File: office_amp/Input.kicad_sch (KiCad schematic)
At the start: 25 parts, among them J2 Conn_01x03_Female, J3 Conn_02x07_Odd_Even, J8 Conn_01x03_Female, K1 EC2-24NU, K2 EC2-24NU, K3 EC2-24NU, K4 EC2-24NU, Q4 BC850, Q5 BC850, U5 MH-M18

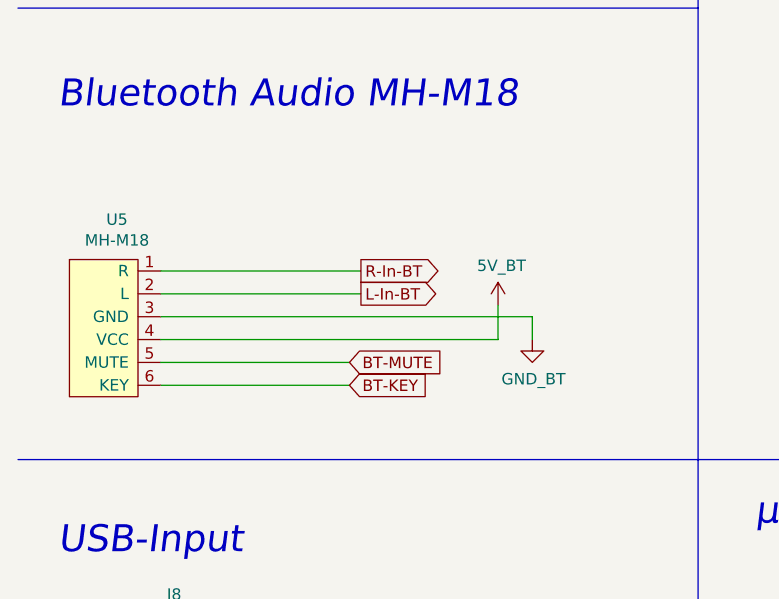
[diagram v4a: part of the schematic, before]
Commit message: Added bluetooth vcc filter, moved i2c pullups to controll board, added touch controller
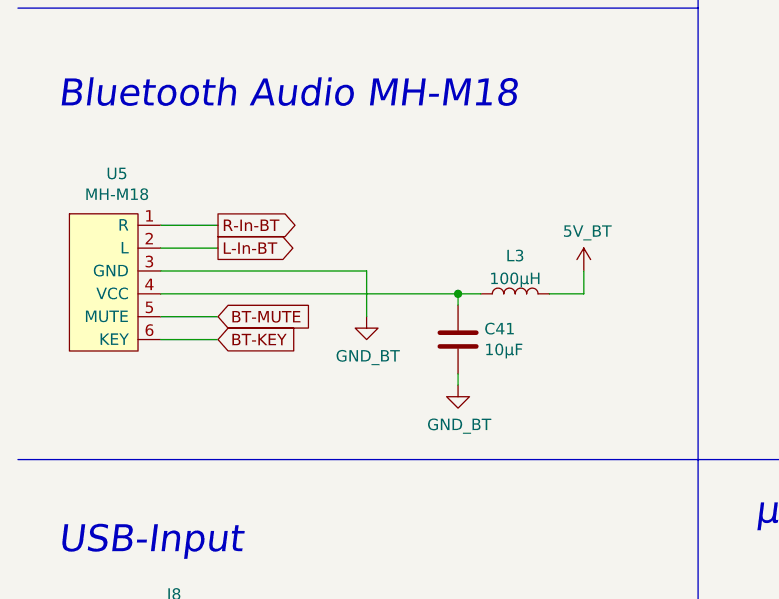
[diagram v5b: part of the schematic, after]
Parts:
- added C41: 10µF, Capacitor_SMD:C_0805_2012Metric_Pad1.18x1.45mm_HandSolder, symbol Device:C
- added L3: 100µH, Inductor_THT:L_Axial_L7.0mm_D3.3mm_P12.70mm_Horizontal_Fastron_MICC, symbol Device:L
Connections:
- net 5V_BT: now also L3.2; no longer U5.4 (VCC)
- net GND_BT: now also C41.2
- new net: C41.1, L3.1, U5.4 (VCC)
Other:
- moved on the sheet: U5

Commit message: Changes from testing
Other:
- note added: "relais in reihe"
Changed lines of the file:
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@@
     (effects (font (size 2.9972 2.9972) italic) (justify left bottom))
+  )
+  (text "relais in reihe" (at 151.765 82.55 0)
+    (effects (font (size 8 8)) (justify left bottom))
   )
   (global_label "L-In-An" (shape output) (at 64.77 35.56 0) (fields_autoplaced)

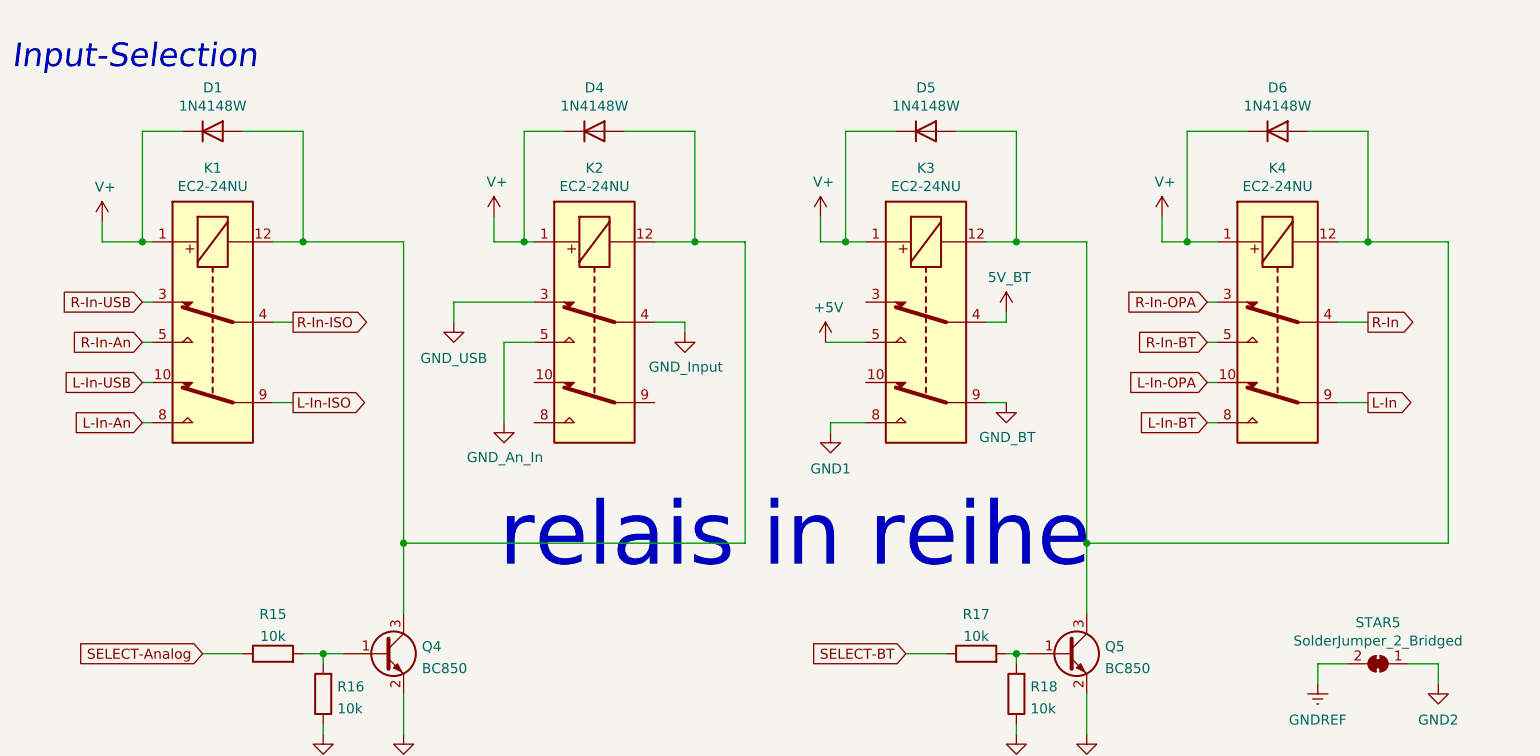
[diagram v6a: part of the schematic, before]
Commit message: Added CHanges from Testing, first layout V1.5
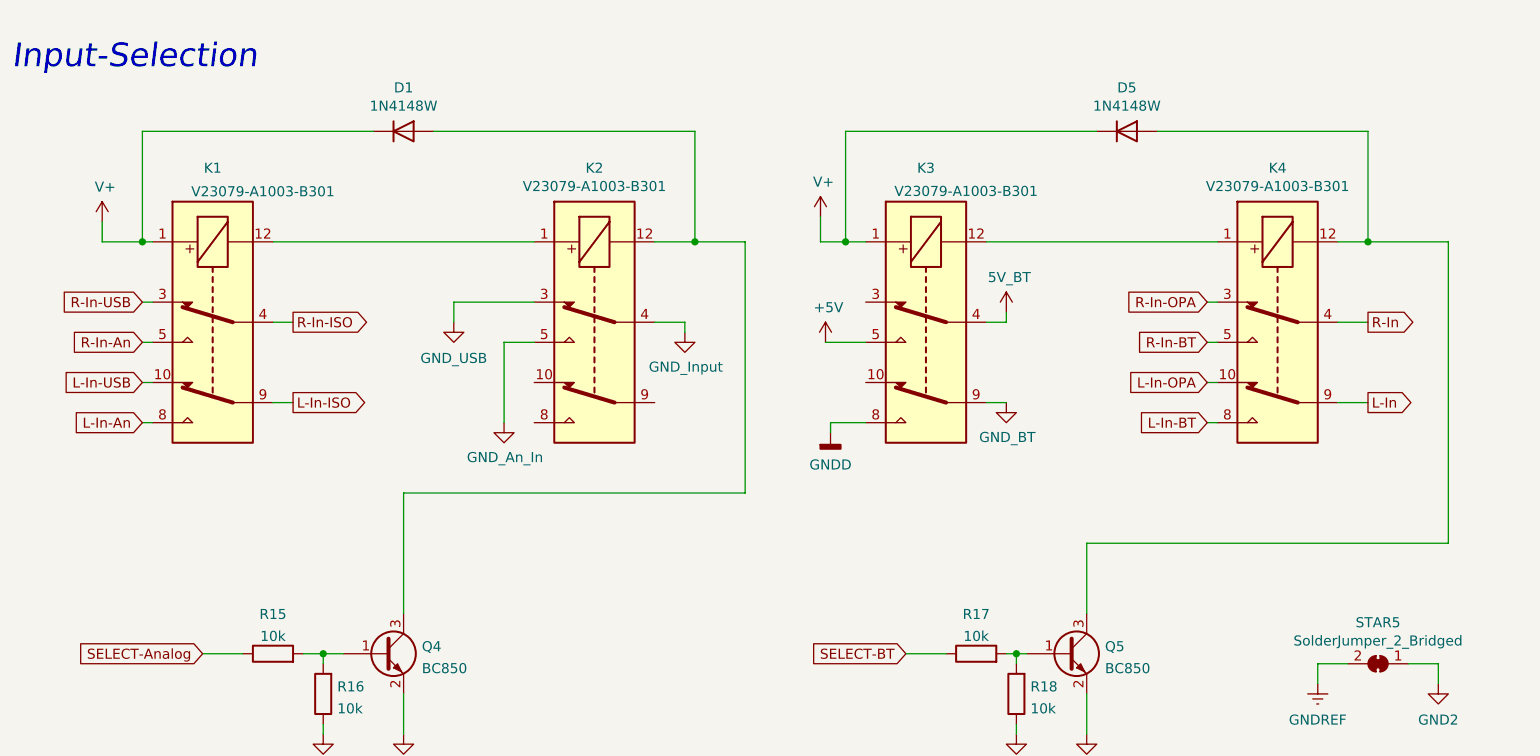
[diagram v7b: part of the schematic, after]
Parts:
- removed D4, D6: 1N4148W, Diode_SMD:D_SOD-123, symbol Diode:1N4148W
- K1, K2, K3, K4: value EC2-24NU -> V23079-A1003-B301
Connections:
- net GND1 is gone; now on net GNDD: K3.8
- net V+: no longer K2.1, K4.1
- net at D1.2 (A), K2.12, Q4.3 (C): no longer K1.12
- net at D5.2 (A), K4.12, Q5.3 (C): no longer K3.12
- new net: K1.12, K2.1
- new net: K3.12, K4.1
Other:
- note removed: "relais in reihe"
- moved on the sheet: D1, D5

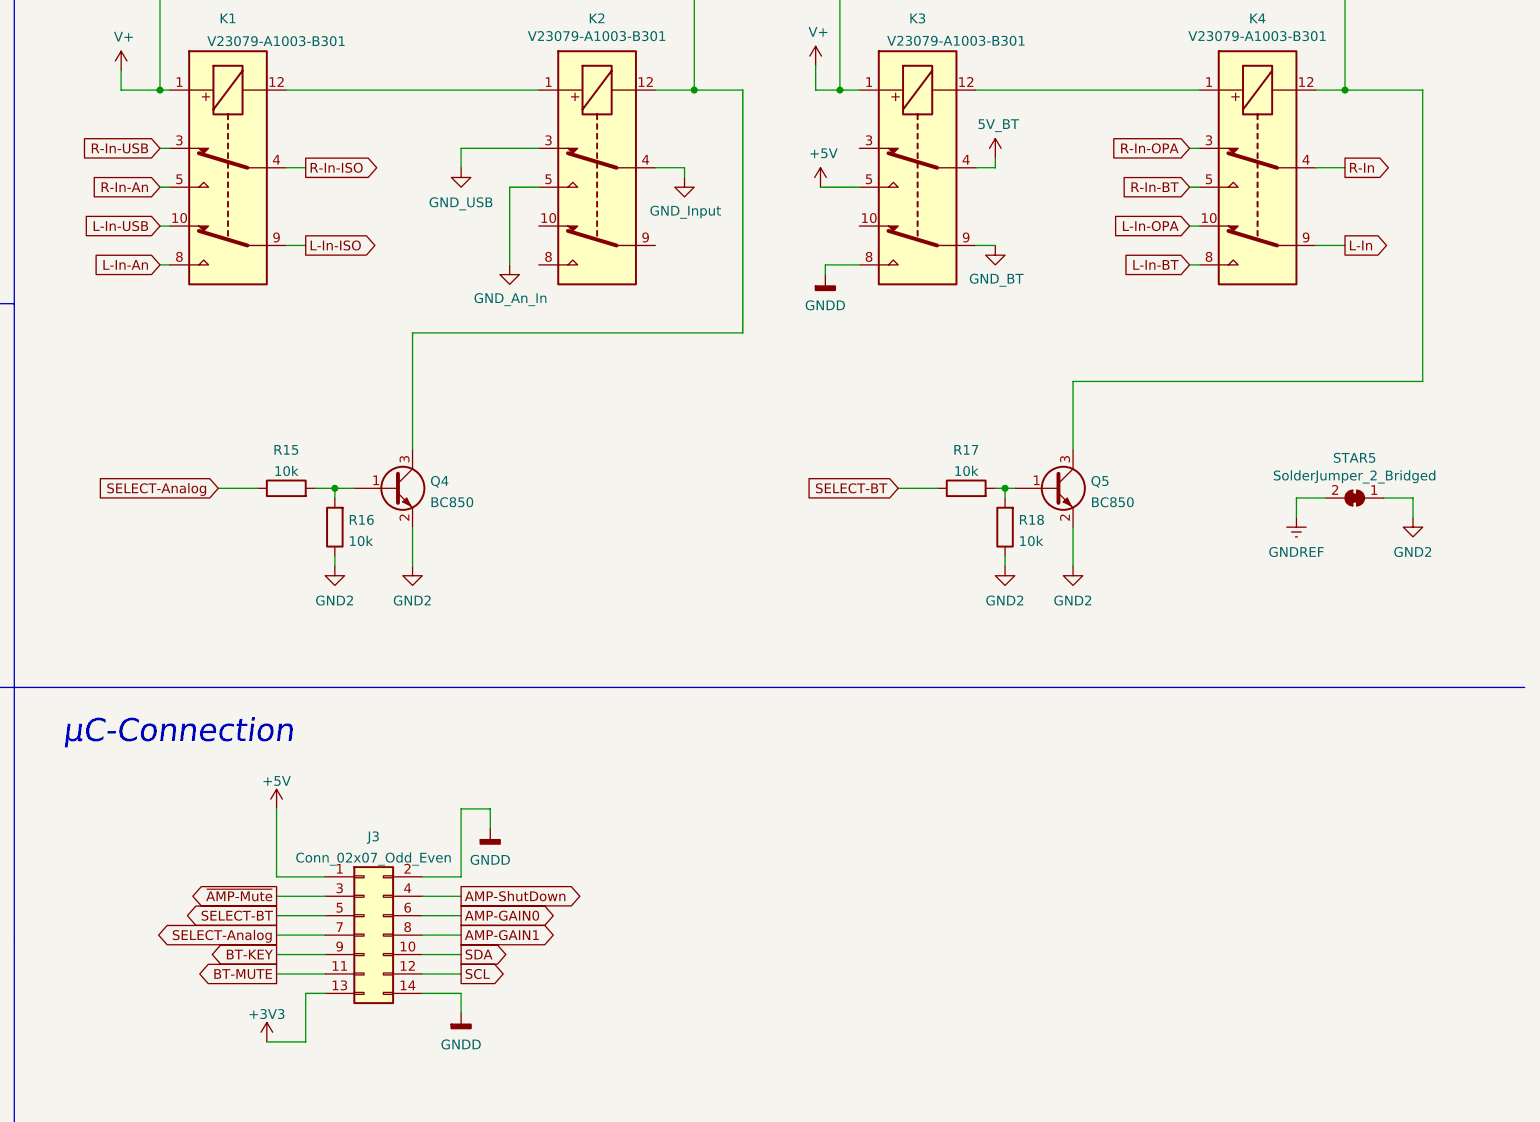
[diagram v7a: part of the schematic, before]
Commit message: Organized Schematic
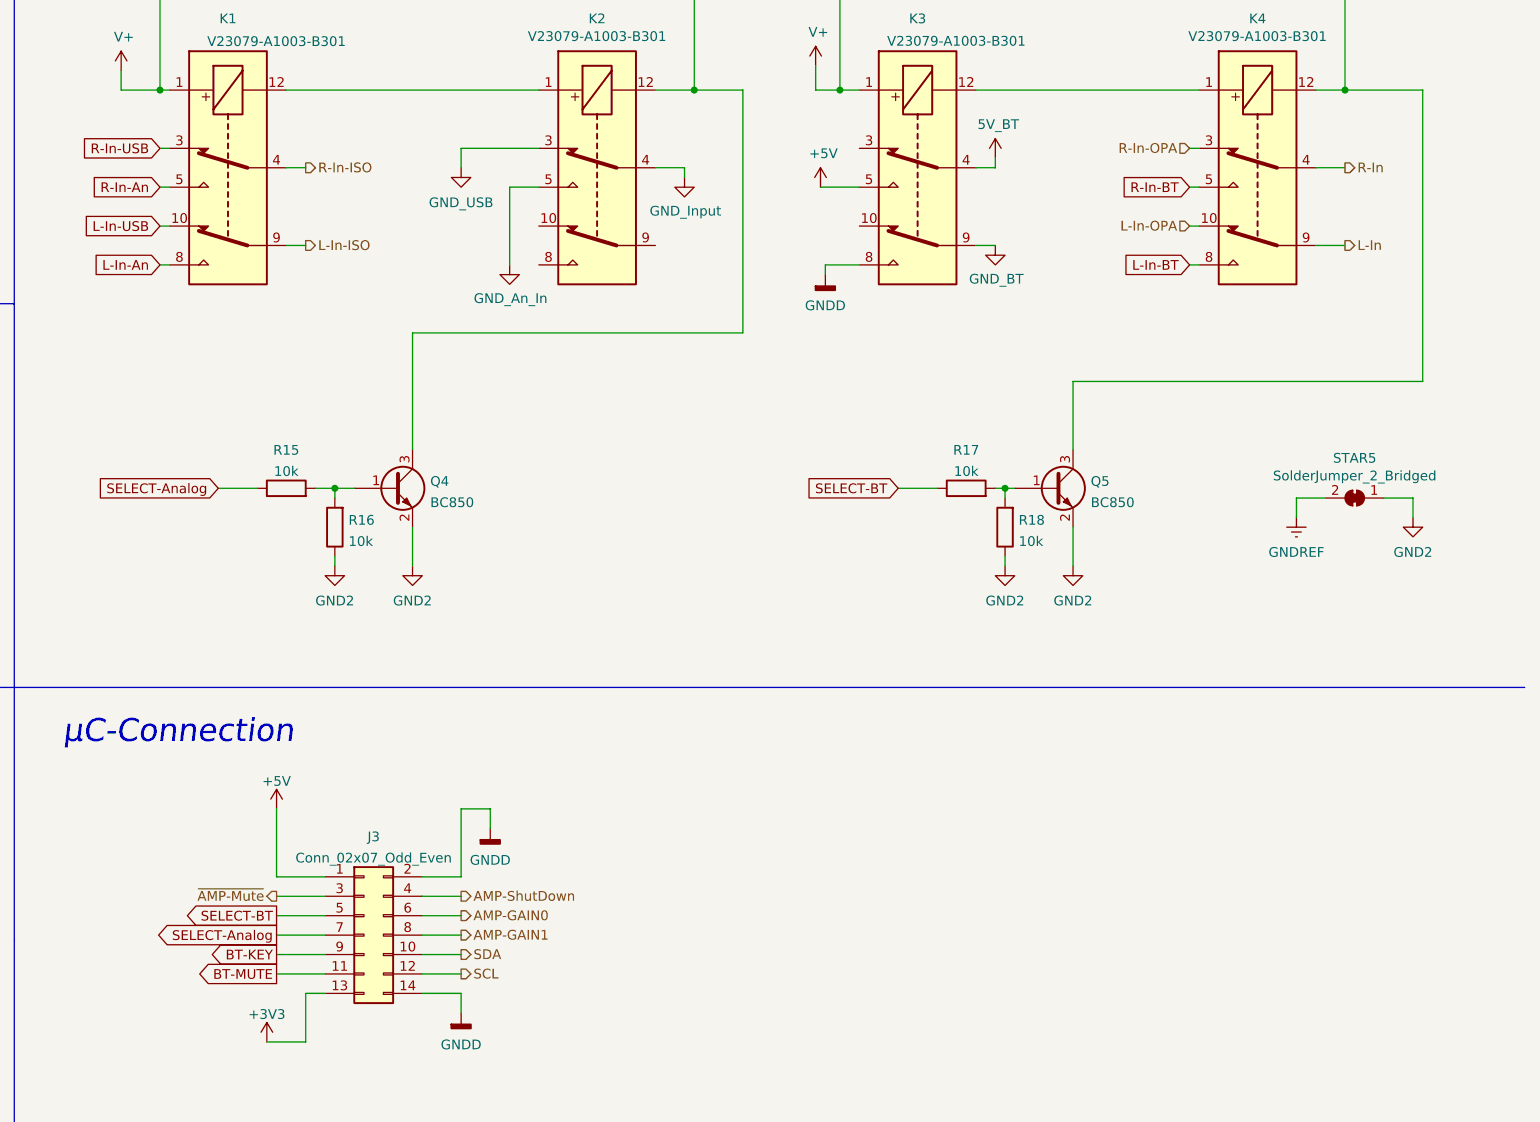
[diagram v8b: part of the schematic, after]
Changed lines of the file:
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@@
-    )
-  )
-  (global_label "SCL" (shape output) (at 146.05 156.21 0) (fields_autoplaced)
-    (effects (font (size 1.27 1.27)) (justify left))
-    (property "Intersheet References" "${INTERSHEET_REFS}" (id 0) (at 151.8818 156.1306 0)
-      (effects (font (size 1.27 1.27)) (justify left) hide)
     )
   )
@@
     )
   )
-  (global_label "R-In-ISO" (shape output) (at 125.73 50.8 0) (fields_autoplaced)
-    (effects (font (size 1.27 1.27)) (justify left))
-    (property "Intersheet References" "${INTERSHEET_REFS}" (id 0) (at -13.97 -16.51 0)
-      (effects (font (size 1.27 1.27)) hide)
-    )
-  )
   (global_label "R-In-BT" (shape output) (at 34.29 92.71 0) (fields_autoplaced)
     (effects (font (size 1.27 1.27)) (justify left))
     (property "Intersheet References" "${INTERSHEET_REFS}" (id 0) (at 0 -5.08 0)
-      (effects (font (size 1.27 1.27)) hide)
-    )
-  )
-  (global_label "R-In-OPA" (shape input) (at 241.3 48.26 180) (fields_autoplaced)
-    (effects (font (size 1.27 1.27)) (justify right))
-    (property "Intersheet References" "${INTERSHEET_REFS}" (id 0) (at 1.27 -16.51 0)
-      (effects (font (size 1.27 1.27)) hide)
-    )
-  )
-  (global_label "L-In-OPA" (shape input) (at 241.3 58.42 180) (fields_autoplaced)
-    (effects (font (size 1.27 1.27)) (justify right))
-    (property "Intersheet References" "${INTERSHEET_REFS}" (id 0) (at 1.27 -16.51 0)
       (effects (font (size 1.27 1.27)) hide)
     )
@@
     (property "Intersheet References" "${INTERSHEET_REFS}" (id 0) (at 13.335 0 0)
       (effects (font (size 1.27 1.27)) hide)
-    )
-  )
-  (global_label "AMP-GAIN1" (shape output) (at 146.05 151.13 0) (fields_autoplaced)
-    (effects (font (size 1.27 1.27)) (justify left))
-    (property "Intersheet References" "${INTERSHEET_REFS}" (id 0) (at 159.2599 151.0506 0)
-      (effects (font (size 1.27 1.27)) (justify left) hide)
     )
   )
@@
     (property "Intersheet References" "${INTERSHEET_REFS}" (id 0) (at -13.97 -16.51 0)
       (effects (font (size 1.27 1.27)) hide)
-    )
-  )
-  (global_label "~{AMP-Mute}" (shape output) (at 121.92 146.05 180) (fields_autoplaced)
-    (effects (font (size 1.27 1.27)) (justify right))
-    (property "Intersheet References" "${INTERSHEET_REFS}" (id 0) (at 109.7987 145.9706 0)
-      (effects (font (size 1.27 1.27)) (justify right) hide)
     )
   )
@@
     (effects (font (size 1.27 1.27)) (justify left))
     (property "Intersheet References" "${INTERSHEET_REFS}" (id 0) (at 13.335 0 0)
-      (effects (font (size 1.27 1.27)) hide)
-    )
-  )
-  (global_label "AMP-ShutDown" (shape output) (at 146.05 146.05 0) (fields_autoplaced)
-    (effects (font (size 1.27 1.27)) (justify left))
-    (property "Intersheet References" "${INTERSHEET_REFS}" (id 0) (at 162.8885 145.9706 0)
-      (effects (font (size 1.27 1.27)) (justify left) hide)
-    )
-  )
-  (global_label "R-In" (shape output) (at 261.62 50.8 0) (fields_autoplaced)
-    (effects (font (size 1.27 1.27)) (justify left))
-    (property "Intersheet References" "${INTERSHEET_REFS}" (id 0) (at 1.27 -16.51 0)
       (effects (font (size 1.27 1.27)) hide)
     )
@@
     )
   )
-  (global_label "L-In-ISO" (shape output) (at 125.73 60.96 0) (fields_autoplaced)
-    (effects (font (size 1.27 1.27)) (justify left))
-    (property "Intersheet References" "${INTERSHEET_REFS}" (id 0) (at -13.97 -16.51 0)
-      (effects (font (size 1.27 1.27)) hide)
-    )
-  )
   (global_label "R-In-BT" (shape input) (at 241.3 53.34 180) (fields_autoplaced)
     (effects (font (size 1.27 1.27)) (justify right))
-    (property "Intersheet References" "${INTERSHEET_REFS}" (id 0) (at 1.27 -16.51 0)
-      (effects (font (size 1.27 1.27)) hide)
-    )
-  )
-  (global_label "L-In" (shape output) (at 261.62 60.96 0) (fields_autoplaced)
-    (effects (font (size 1.27 1.27)) (justify left))
     (property "Intersheet References" "${INTERSHEET_REFS}" (id 0) (at 1.27 -16.51 0)
       (effects (font (size 1.27 1.27)) hide)
@@
     )
   )
-  (global_label "AMP-GAIN0" (shape output) (at 146.05 148.59 0) (fields_autoplaced)
+  (hierarchical_label "R-In" (shape output) (at 261.62 50.8 0)
     (effects (font (size 1.27 1.27)) (justify left))
-    (property "Intersheet References" "${INTERSHEET_REFS}" (id 0) (at 159.2599 148.5106 0)
-      (effects (font (size 1.27 1.27)) (justify left) hide)
-    )
   )
-  (global_label "SDA" (shape output) (at 146.05 153.67 0) (fields_autoplaced)
+  (hierarchical_label "~{AMP-Mute}" (shape output) (at 121.92 146.05 180)
+    (effects (font (size 1.27 1.27)) (justify right))
+  )
+  (hierarchical_label "SCL" (shape output) (at 146.05 156.21 0)
     (effects (font (size 1.27 1.27)) (justify left))
-    (property "Intersheet References" "${INTERSHEET_REFS}" (id 0) (at 151.9423 153.5906 0)
-      (effects (font (size 1.27 1.27)) (justify left) hide)
-    )
+  )
+  (hierarchical_label "R-In-ISO" (shape output) (at 125.73 50.8 0)
+    (effects (font (size 1.27 1.27)) (justify left))
+  )
+  (hierarchical_label "AMP-ShutDown" (shape output) (at 146.05 146.05 0)
+    (effects (font (size 1.27 1.27)) (justify left))
+  )
+  (hierarchical_label "R-In-OPA" (shape input) (at 241.3 48.26 180)
+    (effects (font (size 1.27 1.27)) (justify right))
+  )
+  (hierarchical_label "L-In" (shape output) (at 261.62 60.96 0)
+    (effects (font (size 1.27 1.27)) (justify left))
+  )
+  (hierarchical_label "SDA" (shape output) (at 146.05 153.67 0)
+    (effects (font (size 1.27 1.27)) (justify left))
+  )
+  (hierarchical_label "L-In-ISO" (shape output) (at 125.73 60.96 0)
+    (effects (font (size 1.27 1.27)) (justify left))
+  )
+  (hierarchical_label "L-In-OPA" (shape input) (at 241.3 58.42 180)
+    (effects (font (size 1.27 1.27)) (justify right))
+  )
+  (hierarchical_label "AMP-GAIN0" (shape output) (at 146.05 148.59 0)
+    (effects (font (size 1.27 1.27)) (justify left))
+  )
+  (hierarchical_label "AMP-GAIN1" (shape output) (at 146.05 151.13 0)
+    (effects (font (size 1.27 1.27)) (justify left))
   )
   (symbol (lib_id "MyLib:MH-M18") (at 21.59 99.06 0) (unit 1)
